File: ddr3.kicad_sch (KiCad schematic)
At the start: 12 parts, among them U1 xc7z010clg400, U2 MT41K256M16TW-107_P

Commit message: feat: finish bank0 & qspi sch design
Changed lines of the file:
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@@
 		(fields_autoplaced yes)
 		(property "Reference" "U1"
-			(at 265.43 74.93 0)
+			(at 248.92 113.0299 0)
 			(show_name no)
 			(do_not_autoplace no)
@@
 					(size 1.524 1.524)
 				)
+				(justify left)
 			)
 		)
 		(property "Value" "xc7z010clg400"
-			(at 265.43 77.47 0)
+			(at 248.92 115.5699 0)
 			(show_name no)
 			(do_not_autoplace no)
@@
 					(size 1.524 1.524)
 				)
+				(justify left)
 			)
 		)

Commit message: feat: finish ddr3 sch design
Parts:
- renumbered C3 to C201, C4 to C202, C2 to C203, C1 to C204, R5 to R201, R3 to R202, R4 to R203, R1 to R204, R2 to R205, R6 to R206, U1 to U101, U2 to U201
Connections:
- net DDR_BA0: now also U201.M2 (BA0)
- net DDR_BA1: now also U201.N8 (BA1)
- net DDR_BA2: now also U201.M3 (BA2)
- net DDR_CKE: now also U201.K9 (CKE)
- net DDR_CLK_N: now also U201.K7 (~{CK})
- net DDR_CLK_P: now also U201.J7 (CK)
- net DDR_DM0: now also U201.E7 (LDM)
- net DDR_DM1: now also U201.D3 (UDM)
- net DDR_DQS0_N: now also U201.G3 (~{LDQS})
- net DDR_DQS0_P: now also U201.F3 (LDQS)
- net DDR_DQS1_N: now also U201.B7 (~{UDQS})
- net DDR_DQS1_P: now also U201.C7 (UDQS)
- net DDR_ODT: now also U201.K1 (ODT)
- net DDR_~{RAS}: now reaches U201.J3 (~{RAS})
- net DDR_~{CAS}: now reaches U201.K3 (~{CAS})
- net DDR_~{CS}: now reaches U201.L2 (~{CS})
- net DDR_~{WE}: now reaches U201.L3 (~{WE})
- net DDR_~{RESET}: now reaches U201.T2 (~{RESET})

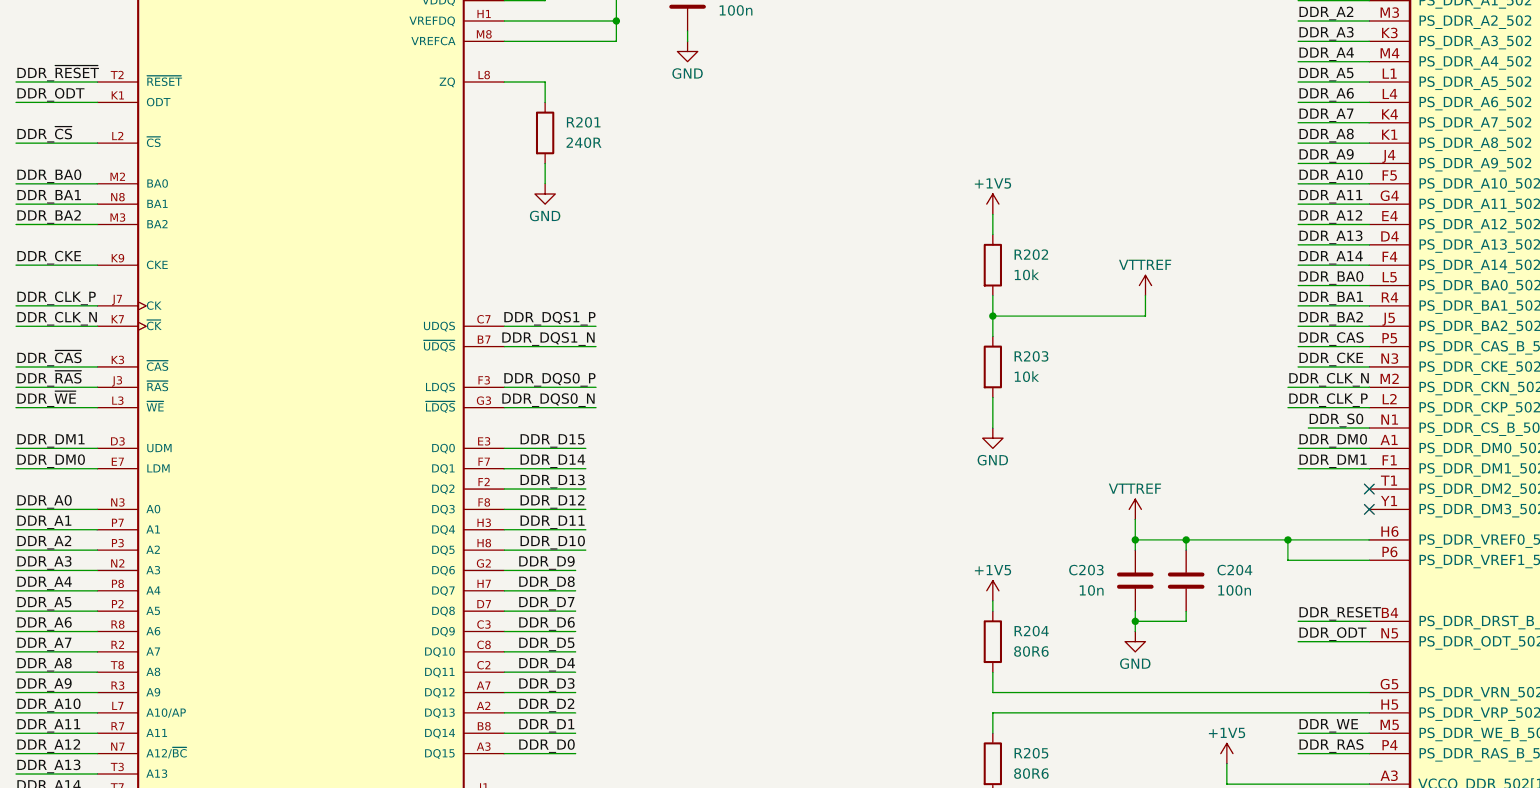
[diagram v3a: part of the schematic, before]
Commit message: feat: start to routing DDR3
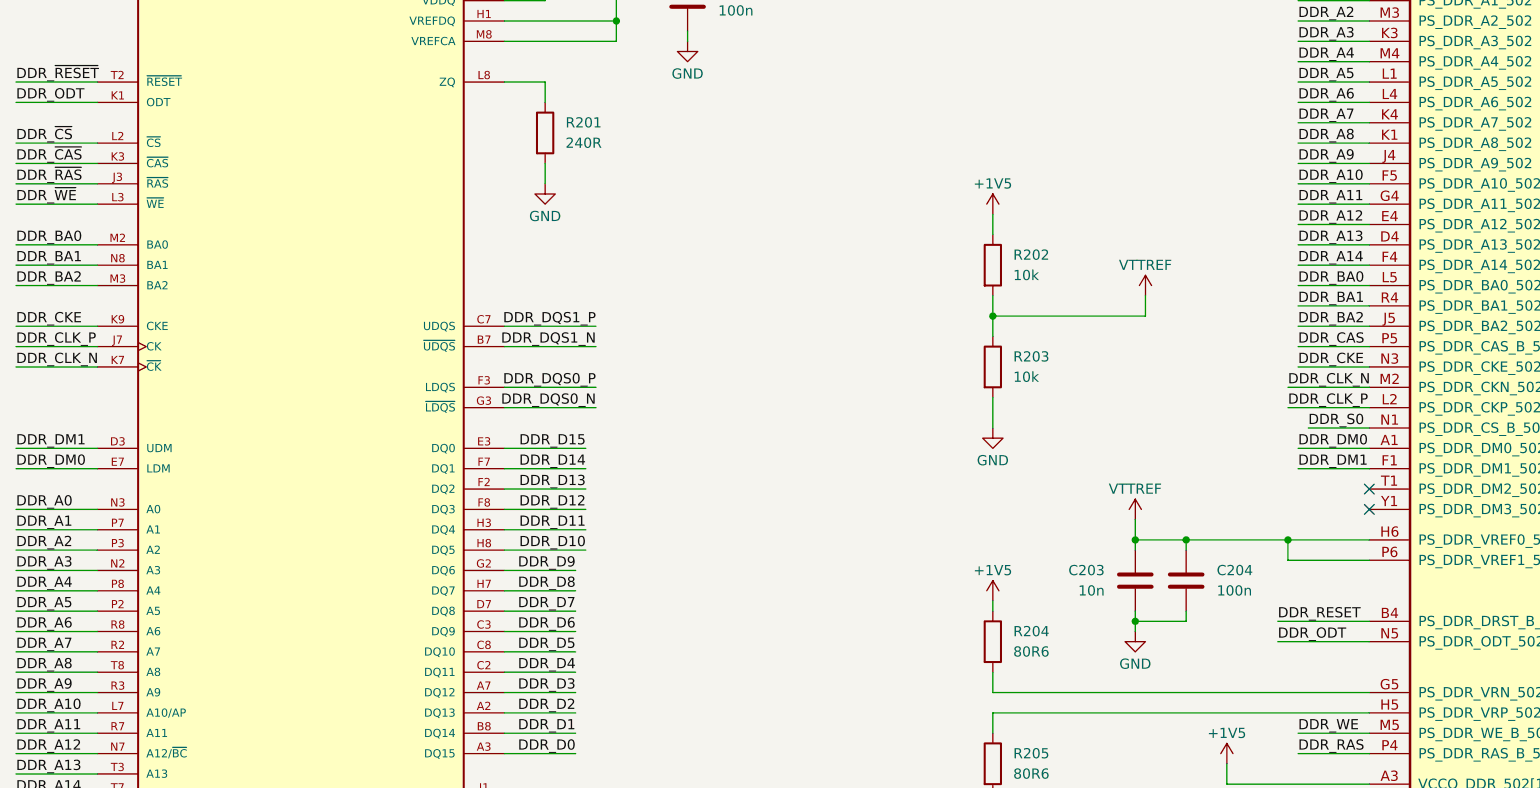
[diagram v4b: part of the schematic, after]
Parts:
- U101: footprint (none) -> Package_BGA:Xilinx_CLG400

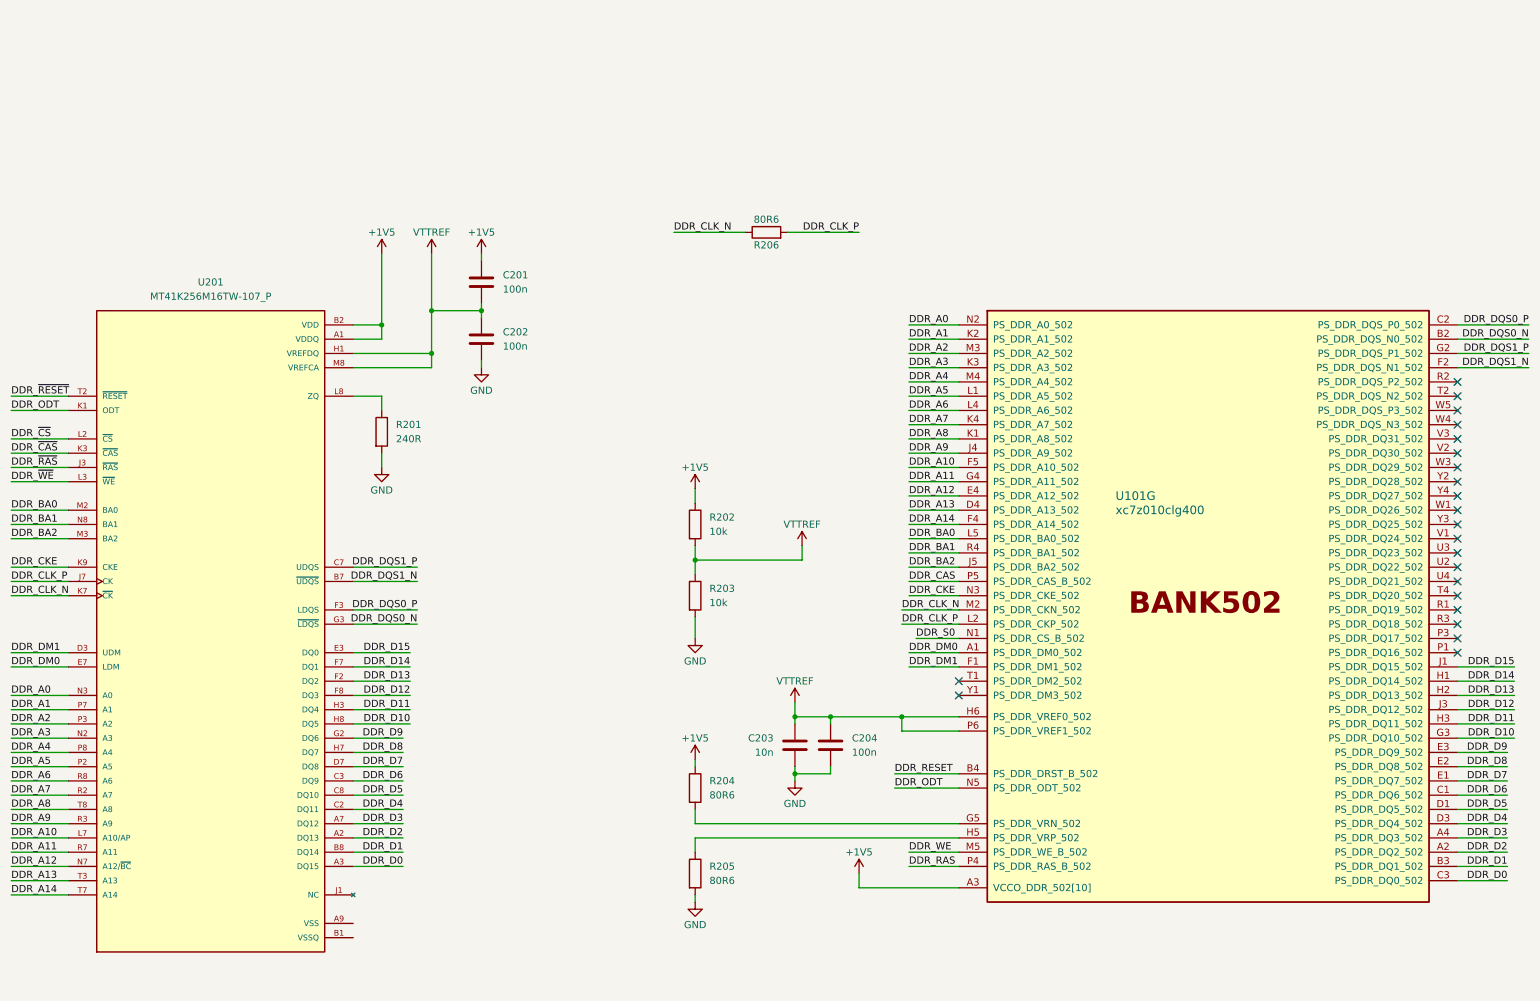
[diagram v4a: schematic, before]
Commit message: feat: restart routing ddr
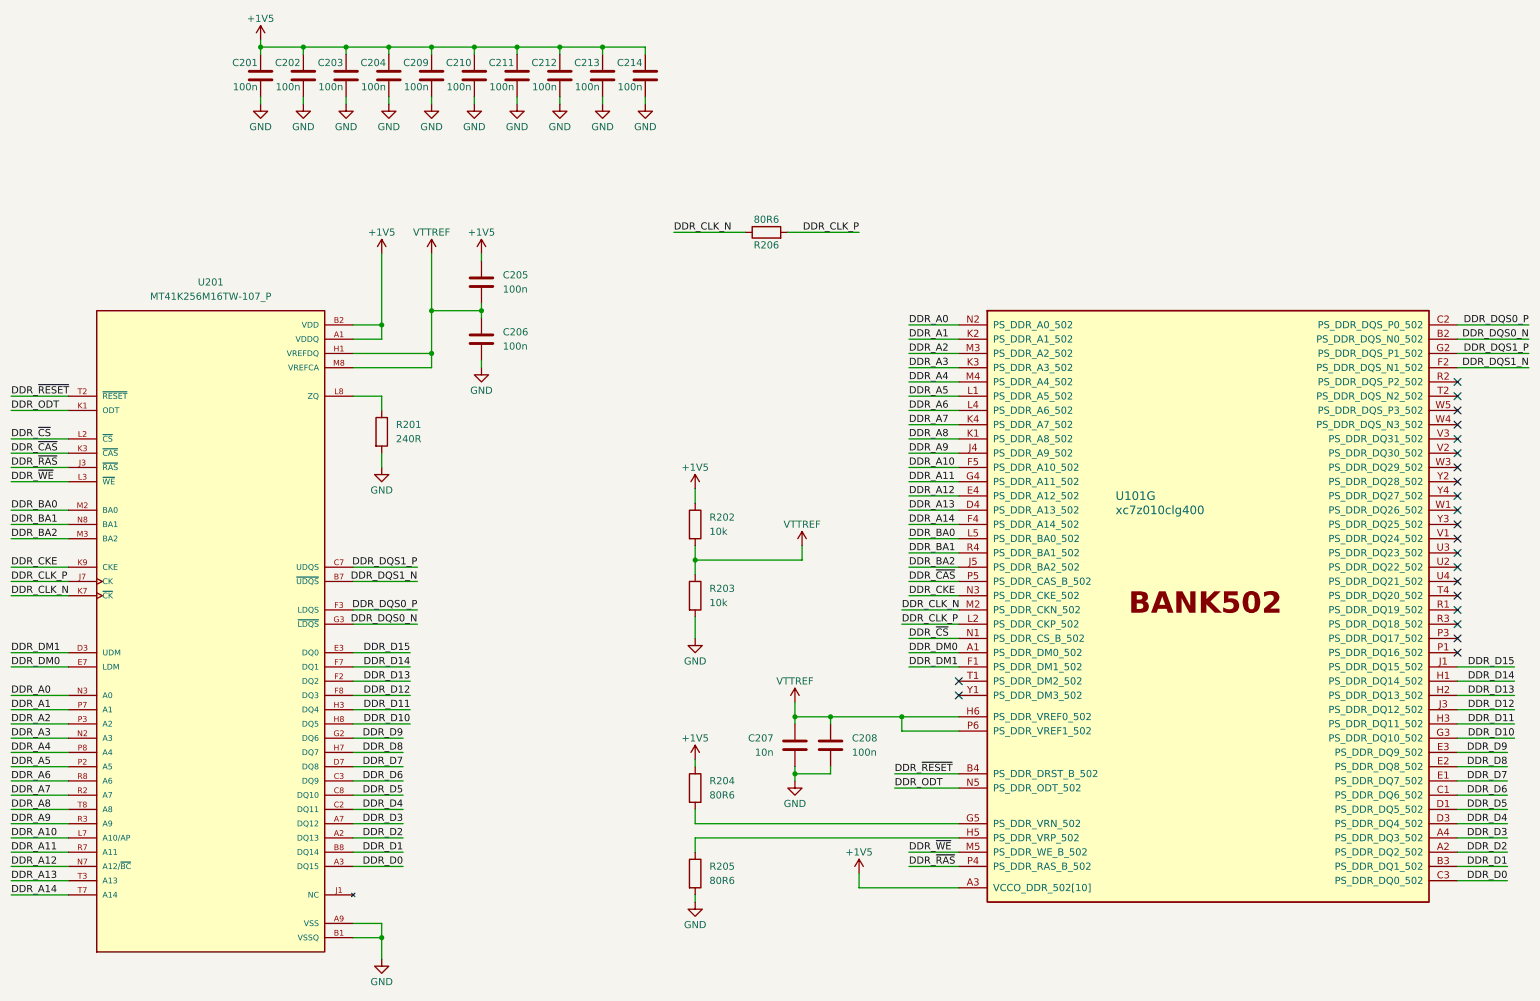
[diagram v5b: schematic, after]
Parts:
- added C201, C202, C203, C204, C209, C210, C211, C212, C213, C214: 100n, Capacitor_SMD:C_0402_1005Metric, symbol Device:C
- C205: renamed from C201; footprint (none) -> Capacitor_SMD:C_0402_1005Metric
- C206: renamed from C202; footprint (none) -> Capacitor_SMD:C_0402_1005Metric
- C208: renamed from C204; footprint (none) -> Capacitor_SMD:C_0402_1005Metric
- R201, R202, R203: footprint (none) -> Resistor_SMD:R_0402_1005Metric
- renumbered C203 to C207
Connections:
- net DDR_CAS is gone; now on net DDR_~{CAS}: U101.P5 (PS_DDR_CAS_B_502)
- net DDR_RAS is gone; now on net DDR_~{RAS}: U101.P4 (PS_DDR_RAS_B_502)
- net DDR_RESET is gone; now on net DDR_~{RESET}: U101.B4 (PS_DDR_DRST_B_502)
- net DDR_S0 is gone; now on net DDR_~{CS}: U101.N1 (PS_DDR_CS_B_502)
- net DDR_WE is gone; now on net DDR_~{WE}: U101.M5 (PS_DDR_WE_B_502)
- net VSS is gone; now on net GND: U201.A9 (VSS), U201.B3 (VSS), U201.E1 (VSS), U201.G8 (VSS), U201.J2 (VSS), U201.J8 (VSS), U201.M1 (VSS), U201.M9 (VSS), U201.P1 (VSS), U201.P9 (VSS), U201.T1 (VSS), U201.T9 (VSS)
- net VSSQ is gone; now on net GND: U201.B1 (VSSQ), U201.B9 (VSSQ), U201.D1 (VSSQ), U201.D8 (VSSQ), U201.E2 (VSSQ), U201.E8 (VSSQ), U201.F9 (VSSQ), U201.G1 (VSSQ), U201.G9 (VSSQ)
- net +1V5: now also C201.1, C202.1, C203.1, C204.1, C209.1, C210.1, C211.1, C212.1, C213.1, C214.1
- net GND: now also C201.2, C202.2, C203.2, C204.2, C209.2, C210.2, C211.2, C212.2, C213.2, C214.2

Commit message: feat: continue routing dd3
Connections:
- net DDR_D0: now also U201.C2 (DQ11); no longer U201.A3 (DQ15)
- net DDR_D1: now also U201.A3 (DQ15); no longer U201.B8 (DQ14)
- net DDR_D10: now also U201.H3 (DQ4); no longer U201.H8 (DQ5)
- net DDR_D11: now also U201.G2 (DQ6); no longer U201.H3 (DQ4)
- net DDR_D13: now also U201.H8 (DQ5); no longer U201.F2 (DQ2)
- net DDR_D2: now also U201.C3 (DQ9); no longer U201.A2 (DQ13)
- net DDR_D3: now also U201.A2 (DQ13); no longer U201.A7 (DQ12)
- net DDR_D4: now also U201.A7 (DQ12); no longer U201.C2 (DQ11)
- net DDR_D6: now also U201.D7 (DQ8); no longer U201.C3 (DQ9)
- net DDR_D7: now also U201.B8 (DQ14); no longer U201.D7 (DQ8)
- net DDR_D9: now also U201.F2 (DQ2); no longer U201.G2 (DQ6)
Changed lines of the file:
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@@
 	(wire
 		(pts
-			(xy 113.03 158.75) (xy 121.92 158.75)
+			(xy 113.03 158.75) (xy 123.19 158.75)
 		)
 		(stroke
@@
 	(wire
 		(pts
-			(xy 113.03 156.21) (xy 121.92 156.21)
+			(xy 113.03 156.21) (xy 123.19 156.21)
 		)
 		(stroke
@@
 	)
 	(label "DDR_D9"
-		(at 121.92 156.21 180)
+		(at 123.19 146.05 180)
 		(effects
 			(font
@@
 	)
 	(label "DDR_D8"
-		(at 121.92 158.75 180)
+		(at 123.19 158.75 180)
 		(effects
 			(font
@@
 	)
 	(label "DDR_D13"
-		(at 123.19 146.05 180)
+		(at 123.19 153.67 180)
 		(effects
 			(font
@@
 	)
 	(label "DDR_D1"
-		(at 121.92 176.53 180)
+		(at 121.92 179.07 180)
 		(effects
 			(font
@@
 	)
 	(label "DDR_D0"
-		(at 121.92 179.07 180)
+		(at 121.92 168.91 180)
 		(effects
 			(font
@@
 	)
 	(label "DDR_D7"
-		(at 121.92 161.29 180)
+		(at 121.92 176.53 180)
 		(effects
 			(font
@@
 	)
 	(label "DDR_D2"
-		(at 121.92 173.99 180)
+		(at 121.92 163.83 180)
 		(effects
 			(font
@@
 	)
 	(label "DDR_D3"
-		(at 121.92 171.45 180)
+		(at 121.92 173.99 180)
 		(effects
 			(font
@@
 	)
 	(label "DDR_D11"
-		(at 123.19 151.13 180)
+		(at 123.19 156.21 180)
 		(effects
 			(font
@@
 	)
 	(label "DDR_D6"
-		(at 121.92 163.83 180)
+		(at 121.92 161.29 180)
 		(effects
 			(font
@@
 	)
 	(label "DDR_D10"
-		(at 123.19 153.67 180)
+		(at 123.19 151.13 180)
 		(effects
 			(font
@@
 	)
 	(label "DDR_D4"
-		(at 121.92 168.91 180)
+		(at 121.92 171.45 180)
 		(effects
 			(font
@@
 	)
 	(group ""
-		(members "0ea18aa6-572c-41a7-9b7e-55c13d7ca2b6" "22e3a5dd-78d9-4f82-9537-8a61ca862c5c"
-			"385f4eee-40e1-48d9-b90d-03e44e99d9fe" "38b37ec3-5648-4d27-b62c-298aae574e4c"
-			"4c78f935-9f6c-4525-93f7-612585ab9ec1" "4fbc5610-1b7a-4c4b-9047-20bff5d9f21e"
-			"62eafbc5-949d-4691-be82-57eed989b5df" "66ab3fb7-af41-479f-a935-99d54adc3428"
-			"7df4e4f2-ca77-4b9d-8f97-3a9430d9ad57" "87525345-a3a3-4604-b121-d916e5133bd1"
-			"9d4ae40b-fa3e-4be9-abb7-ed592576c7a5" "a737a4bb-3876-4499-9176-7387c56e1046"
-			"c2acb322-3368-45a5-86f8-366eafb8035f" "c6b830e4-9413-40b1-910f-1dfceb6936d3"
-			"cd5cc96d-56ba-45d7-9e82-ba170aafe6fb"
+		(members "0ea18aa6-572c-41a7-9b7e-55c13d7ca2b6" "1d8b1c77-f708-484e-8cb8-ad08800afe78"
+			"22e3a5dd-78d9-4f82-9537-8a61ca862c5c" "385f4eee-40e1-48d9-b90d-03e44e99d9fe"
+			"38b37ec3-5648-4d27-b62c-298aae574e4c" "4c78f935-9f6c-4525-93f7-612585ab9ec1"
+			"4fbc5610-1b7a-4c4b-9047-20bff5d9f21e" "62eafbc5-949d-4691-be82-57eed989b5df"
+			"66ab3fb7-af41-479f-a935-99d54adc3428" "7df4e4f2-ca77-4b9d-8f97-3a9430d9ad57"
+			"87525345-a3a3-4604-b121-d916e5133bd1" "9d4ae40b-fa3e-4be9-abb7-ed592576c7a5"
+			"a737a4bb-3876-4499-9176-7387c56e1046" "c2acb322-3368-45a5-86f8-366eafb8035f"
+			"c6b830e4-9413-40b1-910f-1dfceb6936d3" "cd5cc96d-56ba-45d7-9e82-ba170aafe6fb"
 		)
 	)

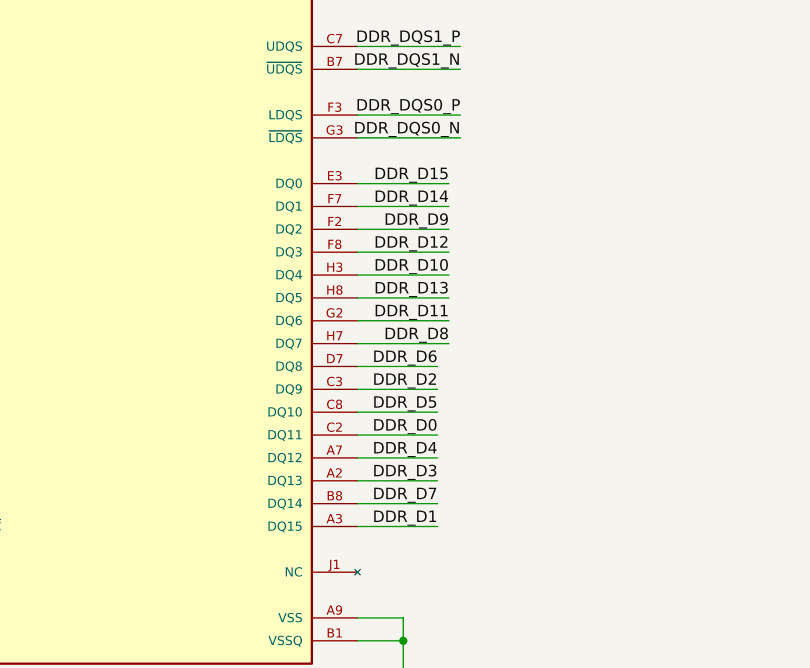
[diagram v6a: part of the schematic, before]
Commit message: feat: continue routing ddr3
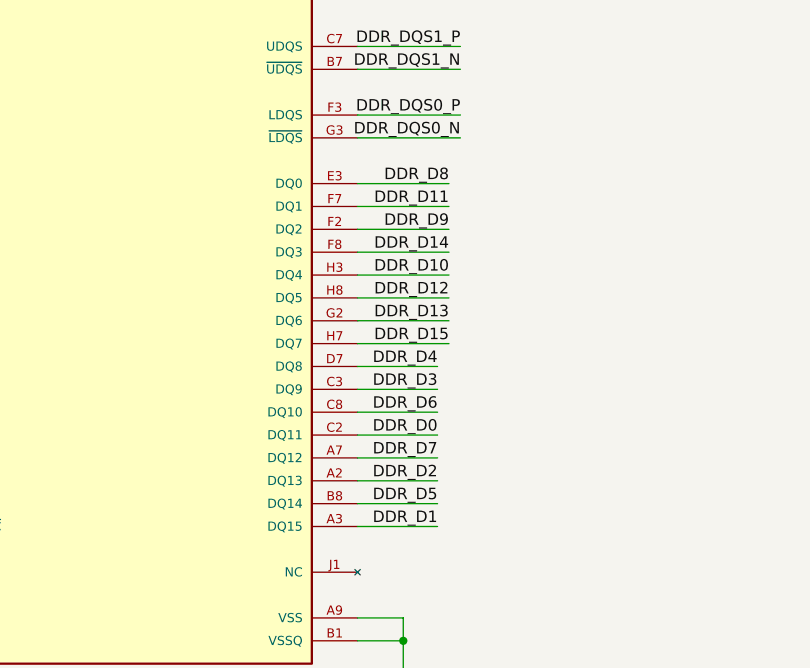
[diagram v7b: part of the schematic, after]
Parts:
- R204, R205: footprint (none) -> Resistor_SMD:R_0402_1005Metric
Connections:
- net DDR_D11: now also U201.F7 (DQ1); no longer U201.G2 (DQ6)
- net DDR_D12: now also U201.H8 (DQ5); no longer U201.F8 (DQ3)
- net DDR_D13: now also U201.G2 (DQ6); no longer U201.H8 (DQ5)
- net DDR_D14: now also U201.F8 (DQ3); no longer U201.F7 (DQ1)
- net DDR_D15: now also U201.H7 (DQ7); no longer U201.E3 (DQ0)
- net DDR_D2: now also U201.A2 (DQ13); no longer U201.C3 (DQ9)
- net DDR_D3: now also U201.C3 (DQ9); no longer U201.A2 (DQ13)
- net DDR_D4: now also U201.D7 (DQ8); no longer U201.A7 (DQ12)
- net DDR_D5: now also U201.B8 (DQ14); no longer U201.C8 (DQ10)
- net DDR_D6: now also U201.C8 (DQ10); no longer U201.D7 (DQ8)
- net DDR_D7: now also U201.A7 (DQ12); no longer U201.B8 (DQ14)
- net DDR_D8: now also U201.E3 (DQ0); no longer U201.H7 (DQ7)
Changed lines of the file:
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@@
 	)
 	(label "DDR_D12"
-		(at 123.19 148.59 180)
+		(at 123.19 153.67 180)
 		(effects
 			(font
@@
 	)
 	(label "DDR_D5"
-		(at 121.92 166.37 180)
+		(at 121.92 176.53 180)
 		(effects
 			(font
@@
 	)
 	(label "DDR_D8"
-		(at 123.19 158.75 180)
+		(at 123.19 140.97 180)
 		(effects
 			(font
@@
 	)
 	(label "DDR_D13"
-		(at 123.19 153.67 180)
+		(at 123.19 156.21 180)
 		(effects
 			(font
@@
 	)
 	(label "DDR_D7"
-		(at 121.92 176.53 180)
+		(at 121.92 171.45 180)
 		(effects
 			(font
@@
 	)
 	(label "DDR_D15"
-		(at 123.19 140.97 180)
+		(at 123.19 158.75 180)
 		(effects
 			(font
@@
 	)
 	(label "DDR_D14"
-		(at 123.19 143.51 180)
+		(at 123.19 148.59 180)
 		(effects
 			(font
@@
 	)
 	(label "DDR_D2"
-		(at 121.92 163.83 180)
+		(at 121.92 173.99 180)
 		(effects
 			(font
@@
 	)
 	(label "DDR_D3"
-		(at 121.92 173.99 180)
+		(at 121.92 163.83 180)
 		(effects
 			(font
@@
 	)
 	(label "DDR_D11"
-		(at 123.19 156.21 180)
+		(at 123.19 143.51 180)
 		(effects
 			(font
@@
 	)
 	(label "DDR_D6"
-		(at 121.92 161.29 180)
+		(at 121.92 166.37 180)
 		(effects
 			(font
@@
 	)
 	(label "DDR_D4"
-		(at 121.92 171.45 180)
+		(at 121.92 161.29 180)
 		(effects
 			(font
@@
 			)
 		)
-		(property "Footprint" ""
+		(property "Footprint" "Resistor_SMD:R_0402_1005Metric"
 			(at 172.212 180.34 90)
 			(hide yes)
@@
 			)
 		)
-		(property "Footprint" ""
+		(property "Footprint" "Resistor_SMD:R_0402_1005Metric"
 			(at 172.212 165.1 90)
 			(hide yes)
